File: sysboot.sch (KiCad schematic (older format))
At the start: 19 parts, among them IC2 AM335X_ZCZ

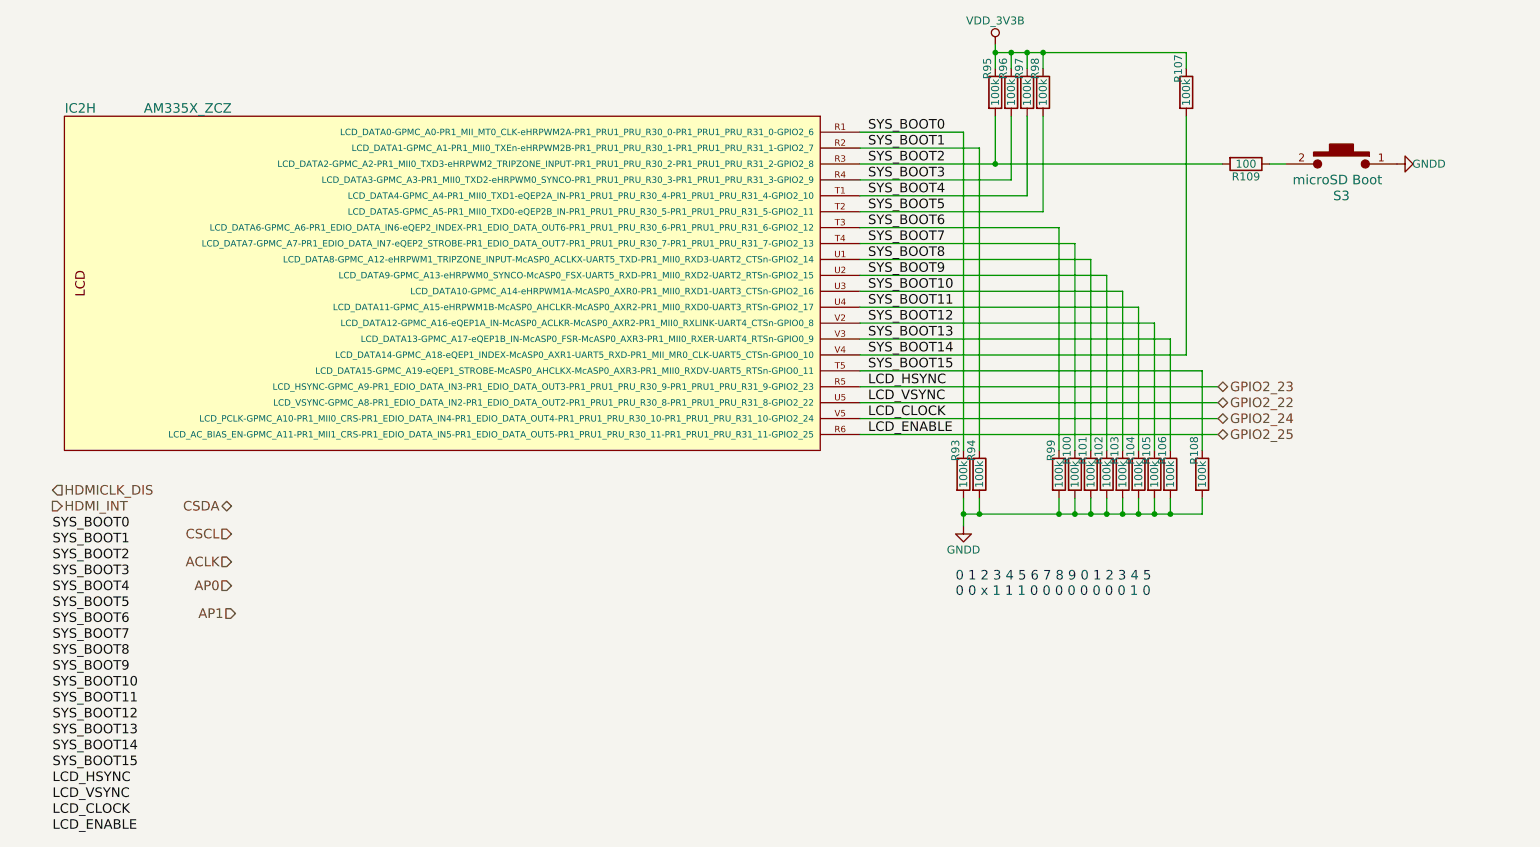
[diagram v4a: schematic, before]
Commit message: add display connector, bom generated, sch second version
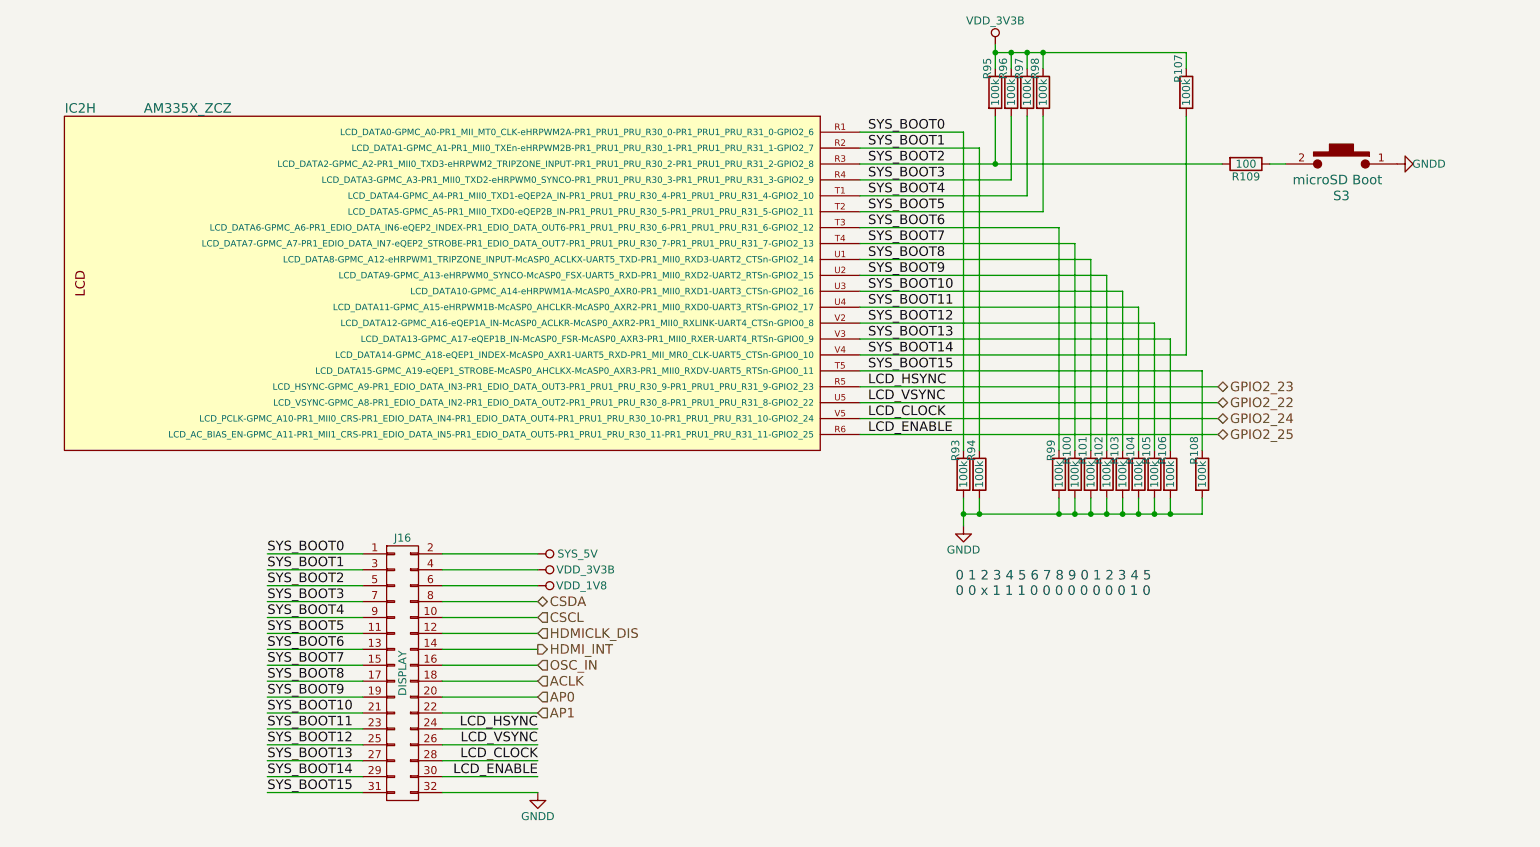
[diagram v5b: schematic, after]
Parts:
- added J16: DISPLAY, symbol CONN_02X16
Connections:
- net ACLK: now also J16.18 (P18)
- net AP0: now also J16.20 (P20)
- net AP1: now also J16.22 (P22)
- net CSCL: now also J16.10 (P10)
- net CSDA: now also J16.8 (P8)
- net GNDD: now also J16.32 (P32)
- net GPIO2_22: now also J16.26 (P26)
- net GPIO2_23: now also J16.24 (P24)
- net GPIO2_24: now also J16.28 (P28)
- net GPIO2_25: now also J16.30 (P30)
- net HDMICLK_DIS: now also J16.12 (P12)
- net HDMI_INT: now also J16.14 (P14)
- net SYS_BOOT0: now also J16.1 (P1)
- net SYS_BOOT1: now also J16.3 (P3)
- net SYS_BOOT10: now also J16.21 (P21)
- net SYS_BOOT11: now also J16.23 (P23)
- net SYS_BOOT12: now also J16.25 (P25)
- net SYS_BOOT13: now also J16.27 (P27)
- net SYS_BOOT14: now also J16.29 (P29)
- net SYS_BOOT15: now also J16.31 (P31)
- net SYS_BOOT2: now also J16.5 (P5)
- net SYS_BOOT3: now also J16.7 (P7)
- net SYS_BOOT4: now also J16.9 (P9)
- net SYS_BOOT5: now also J16.11 (P11)
- net SYS_BOOT6: now also J16.13 (P13)
- net SYS_BOOT7: now also J16.15 (P15)
- net SYS_BOOT8: now also J16.17 (P17)
- net SYS_BOOT9: now also J16.19 (P19)
- net VDD_3V3B: now also J16.4 (P4)
- new net OSC_IN: J16.16 (P16)
- new net SYS_5V: J16.2 (P2)
- new net VDD_1V8: J16.6 (P6)
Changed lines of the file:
@@
 $EndComp
 Wire Wire Line
-	6800 4750 6800 4850
-Wire Wire Line
-	6800 4850 6800 4925
+	6800 4750 6800 4925
 Wire Wire Line
 	8300 4850 8300 4750
@@
 Connection ~ 6900 4850
 Wire Wire Line
-	6800 4850 6900 4850
-Wire Wire Line
-	6900 4850 7400 4850
-Wire Wire Line
-	7400 4850 7500 4850
-Wire Wire Line
-	7500 4850 7600 4850
-Wire Wire Line
-	7600 4850 7700 4850
-Wire Wire Line
-	7700 4850 7800 4850
-Wire Wire Line
-	7800 4850 7900 4850
-Wire Wire Line
-	7900 4850 8000 4850
-Wire Wire Line
-	8000 4850 8100 4850
-Wire Wire Line
-	8100 4850 8300 4850
+	6800 4850 8300 4850
 Wire Wire Line
 	8200 1950 8200 2050
@@
 Connection ~ 7100 1950
 Wire Wire Line
-	7000 1900 7000 1950
-Wire Wire Line
-	7000 1950 7000 2050
+	7000 1900 7000 2050
 Connection ~ 7000 1950
 $Comp
@@
 	6900 2550 6150 2550
 Wire Wire Line
-	6150 2650 7000 2650
-Wire Wire Line
-	7000 2650 8425 2650
+	6150 2650 8425 2650
 Connection ~ 7000 2650
 Wire Wire Line
@@
 	7200 2850 7200 2350
 Wire Wire Line
-	7000 1950 7100 1950
-Wire Wire Line
-	7100 1950 7200 1950
-Wire Wire Line
-	7200 1950 7300 1950
-Wire Wire Line
-	7300 1950 8200 1950
+	7000 1950 8200 1950
 Text HLabel 8400 4050 2    60   BiDi ~ 0
 GPIO2_23
@@
 Text Label 6200 4350 0    60   ~ 0
 LCD_ENABLE
-Text Label 1075 4950 0    60   ~ 0
+Text Label 2425 5100 0    60   ~ 0
 SYS_BOOT0
-Text Label 1075 5050 0    60   ~ 0
+Text Label 2425 5200 0    60   ~ 0
 SYS_BOOT1
-Text Label 1075 5150 0    60   ~ 0
+Text Label 2425 5300 0    60   ~ 0
 SYS_BOOT2
-Text Label 1075 5250 0    60   ~ 0
+Text Label 2425 5400 0    60   ~ 0
 SYS_BOOT3
-Text Label 1075 5350 0    60   ~ 0
+Text Label 2425 5500 0    60   ~ 0
 SYS_BOOT4
-Text Label 1075 5450 0    60   ~ 0
+Text Label 2425 5600 0    60   ~ 0
 SYS_BOOT5
-Text Label 1075 5550 0    60   ~ 0
+Text Label 2425 5700 0    60   ~ 0
 SYS_BOOT6
-Text Label 1075 5650 0    60   ~ 0
+Text Label 2425 5800 0    60   ~ 0
 SYS_BOOT7
-Text Label 1075 5750 0    60   ~ 0
+Text Label 2425 5900 0    60   ~ 0
 SYS_BOOT8
-Text Label 1075 5850 0    60   ~ 0
+Text Label 2425 6000 0    60   ~ 0
 SYS_BOOT9
-Text Label 1075 5950 0    60   ~ 0
+Text Label 2425 6100 0    60   ~ 0
 SYS_BOOT10
-Text Label 1075 6050 0    60   ~ 0
+Text Label 2425 6200 0    60   ~ 0
 SYS_BOOT11
-Text Label 1075 6150 0    60   ~ 0
+Text Label 2425 6300 0    60   ~ 0
 SYS_BOOT12
-Text Label 1075 6250 0    60   ~ 0
+Text Label 2425 6400 0    60   ~ 0
 SYS_BOOT13
-Text Label 1075 6350 0    60   ~ 0
+Text Label 2425 6500 0    60   ~ 0
 SYS_BOOT14
-Text Label 1075 6450 0    60   ~ 0
+Text Label 2425 6600 0    60   ~ 0
 SYS_BOOT15
-Text Label 1075 6550 0    60   ~ 0
+Text Label 4125 6200 2    60   ~ 0
 LCD_HSYNC
-Text Label 1075 6650 0    60   ~ 0
+Text Label 4125 6300 2    60   ~ 0
 LCD_VSYNC
-Text Label 1075 6750 0    60   ~ 0
+Text Label 4125 6400 2    60   ~ 0
 LCD_CLOCK
-Text Label 1075 6850 0    60   ~ 0
+Text Label 4125 6500 2    60   ~ 0
 LCD_ENABLE
-Text HLabel 1075 4800 2    60   Output ~ 0
+Text HLabel 4125 5700 2    60   Output ~ 0
 HDMI_INT
-Text HLabel 2200 4800 0    60   BiDi ~ 0
+Text HLabel 4125 5400 2    60   BiDi ~ 0
 CSDA
-Text HLabel 2200 4975 0    60   Input ~ 0
+Text HLabel 4125 5500 2    60   Input ~ 0
 CSCL
-Text HLabel 2200 5150 0    60   Input ~ 0
+Text HLabel 4125 5900 2    60   Input ~ 0
 ACLK
-Text HLabel 2200 5300 0    60   Input ~ 0
+Text HLabel 4125 6000 2    60   Input ~ 0
 AP0
-Text HLabel 2225 5475 0    60   Input ~ 0
+Text HLabel 4125 6100 2    60   Input ~ 0
 AP1
-Text HLabel 1075 4700 2    60   Input ~ 0
+Text HLabel 4125 5600 2    60   Input ~ 0
 HDMICLK_DIS
+$Comp
+L VDD_1V8 #PWR0322
+U 1 1 58CC8C97
+P 4125 5300
+F 0 "#PWR0322" H 4125 5150 50  0001 C CNN
+F 1 "VDD_1V8" V 4125 5575 50  0000 C CNN
+F 2 "" H 4125 5300 50  0000 C CNN
+F 3 "" H 4125 5300 50  0000 C CNN
+	1    4125 5300
+	0    1    1    0
+$EndComp
+$Comp
+L VDD_3V3B #PWR0323
+U 1 1 58CC8D56
+P 4125 5200
+F 0 "#PWR0323" H 4125 5050 50  0001 C CNN
+F 1 "VDD_3V3B" V 4125 5500 50  0000 C CNN
+F 2 "" H 4125 5200 50  0000 C CNN
+F 3 "" H 4125 5200 50  0000 C CNN
+	1    4125 5200
+	0    1    1    0
+$EndComp
+$Comp
+L GNDD #PWR0324
+U 1 1 58CC8E02
+P 4125 6600
+F 0 "#PWR0324" H 4125 6350 50  0001 C CNN
+F 1 "GNDD" H 4125 6450 50  0000 C CNN
+F 2 "" H 4125 6600 50  0001 C CNN
+F 3 "" H 4125 6600 50  0001 C CNN
+	1    4125 6600
+	1    0    0    -1
+$EndComp
+$Comp
+L SYS_5V #PWR0325
+U 1 1 58CC8E3C
+P 4125 5100
+F 0 "#PWR0325" H 4125 4950 50  0001 C CNN
+F 1 "SYS_5V" V 4125 5350 50  0000 C CNN
+F 2 "" H 4125 5100 50  0000 C CNN
+F 3 "" H 4125 5100 50  0000 C CNN
+	1    4125 5100
+	0    1    1    0
+$EndComp
+Text HLabel 4125 5800 2    60   Input ~ 0
+OSC_IN
+$Comp
+L CONN_02X16 J16
+U 1 1 58CD9683
+P 3275 5850
+F 0 "J16" H 3275 6700 50  0000 C CNN
+F 1 "DISPLAY" V 3275 5850 50  0000 C CNN
+F 2 "" H 3275 4750 50  0001 C CNN
+F 3 "" H 3275 4750 50  0001 C CNN
+	1    3275 5850
+	1    0    0    -1
+$EndComp
+Wire Wire Line
+	2425 5100 3025 5100
+Wire Wire Line
+	2425 5200 3025 5200
+Wire Wire Line
+	2425 5300 3025 5300
+Wire Wire Line
+	2425 5400 3025 5400
+Wire Wire Line
+	2425 5500 3025 5500
+Wire Wire Line
+	2425 5600 3025 5600
+Wire Wire Line
+	2425 5700 3025 5700
+Wire Wire Line
+	2425 5800 3025 5800
+Wire Wire Line
+	2425 5900 3025 5900
+Wire Wire Line
+	2425 6000 3025 6000
+Wire Wire Line
+	2425 6100 3025 6100
+Wire Wire Line
+	2425 6200 3025 6200
+Wire Wire Line
+	2425 6300 3025 6300
+Wire Wire Line
+	2425 6400 3025 6400
+Wire Wire Line
+	2425 6500 3025 6500
+Wire Wire Line
+	2425 6600 3025 6600
+Wire Wire Line
+	3525 5100 4125 5100
+Wire Wire Line
+	3525 5200 4125 5200
+Wire Wire Line
+	3525 5300 4125 5300
+Wire Wire Line
+	3525 5400 4125 5400
+Wire Wire Line
+	3525 5500 4125 5500
+Wire Wire Line
+	3525 5600 4125 5600
+Wire Wire Line
+	3525 5700 4125 5700
+Wire Wire Line
+	3525 5800 4125 5800
+Wire Wire Line
+	3525 5900 4125 5900
+Wire Wire Line
+	3525 6000 4125 6000
+Wire Wire Line
+	3525 6100 4125 6100
+Wire Wire Line
+	3525 6200 4125 6200
+Wire Wire Line
+	3525 6300 4125 6300
+Wire Wire Line
+	3525 6400 4125 6400
+Wire Wire Line
+	3525 6500 4125 6500
+Wire Wire Line
+	3525 6600 4125 6600
 $EndSCHEMATC
